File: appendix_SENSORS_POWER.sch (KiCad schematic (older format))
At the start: 18 parts

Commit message: pre Annotation 1
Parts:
- removed C? (x2): 10u, symbol Device:C
- removed R? (x2): 4k7, symbol Device:R
- added C? (x2): 10u, symbol Device:C
- added R? (x3): nc, symbol Device:R
- added R? (x2): 10k, symbol Device:R
- R?: value 4k7 -> 10k
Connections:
- wire segments 81 -> 72
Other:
- note added: "Connectors are missing"
- note added: "select\n- pull-up\n- pull-down"
- note removed: "- Stecker von Tobi\n"
- moved on the sheet: C?, R?

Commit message: 1st annotation, footprints, netlist
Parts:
- C401, C402, C403, C404, C405, C406: renamed from C?; footprint (none) -> Capacitors_SMD:C_0805
- R401, R402, R403, R404, R405, R406, R407, R408, R409, R410, R411, R412: renamed from R?; footprint (none) -> Resistors_SMD:R_0805
- T401, T402, T403: renamed from T?; footprint (none) -> Silicon-Standard:TO-263_D2PAK

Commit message: started layouting TMC2660
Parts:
- C401, C402, C403, C404, C405, C406: footprint Capacitors_SMD:C_0805 -> Capacitors_SMD:C_0603
- R401, R402, R403, R404, R405, R406, R407, R408, R409, R410, R411, R412: footprint Resistors_SMD:R_0805 -> Resistors_SMD:R_0603
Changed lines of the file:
@@
 F 0 "C402" H 4965 1846 50  0000 L CNN
 F 1 "10u" H 4965 1755 50  0000 L CNN
-F 2 "Capacitors_SMD:C_0805" H 4888 1650 50  0001 C CNN
+F 2 "Capacitors_SMD:C_0603" H 4888 1650 50  0001 C CNN
 F 3 "~" H 4850 1800 50  0001 C CNN
 	1    4850 1800
@@
 F 0 "R402" H 4570 1346 50  0000 L CNN
 F 1 "10k" H 4570 1255 50  0000 L CNN
-F 2 "Resistors_SMD:R_0805" V 4430 1300 50  0001 C CNN
+F 2 "Resistors_SMD:R_0603" V 4430 1300 50  0001 C CNN
 F 3 "~" H 4500 1300 50  0001 C CNN
 	1    4500 1300
@@
 F 0 "R404" V 8343 1800 50  0000 C CNN
 F 1 "10k" V 8434 1800 50  0000 C CNN
-F 2 "Resistors_SMD:R_0805" V 8480 1800 50  0001 C CNN
+F 2 "Resistors_SMD:R_0603" V 8480 1800 50  0001 C CNN
 F 3 "~" H 8550 1800 50  0001 C CNN
 	1    8550 1800
@@
 F 0 "R407" V 8343 3150 50  0000 C CNN
 F 1 "10k" V 8434 3150 50  0000 C CNN
-F 2 "Resistors_SMD:R_0805" V 8480 3150 50  0001 C CNN
+F 2 "Resistors_SMD:R_0603" V 8480 3150 50  0001 C CNN
 F 3 "~" H 8550 3150 50  0001 C CNN
 	1    8550 3150
@@
 F 0 "R411" V 8343 4500 50  0000 C CNN
 F 1 "10k" V 8434 4500 50  0000 C CNN
-F 2 "Resistors_SMD:R_0805" V 8480 4500 50  0001 C CNN
+F 2 "Resistors_SMD:R_0603" V 8480 4500 50  0001 C CNN
 F 3 "~" H 8550 4500 50  0001 C CNN
 	1    8550 4500
@@
 F 0 "R403" H 4570 1846 50  0000 L CNN
 F 1 "nc" H 4570 1755 50  0000 L CNN
-F 2 "Resistors_SMD:R_0805" V 4430 1800 50  0001 C CNN
+F 2 "Resistors_SMD:R_0603" V 4430 1800 50  0001 C CNN
 F 3 "~" H 4500 1800 50  0001 C CNN
 	1    4500 1800
@@
 F 0 "R409" H 1820 4346 50  0000 L CNN
 F 1 "4k7" H 1820 4255 50  0000 L CNN
-F 2 "Resistors_SMD:R_0805" V 1680 4300 50  0001 C CNN
+F 2 "Resistors_SMD:R_0603" V 1680 4300 50  0001 C CNN
 F 3 "~" H 1750 4300 50  0001 C CNN
 	1    1750 4300
@@
 F 0 "C405" H 1865 4846 50  0000 L CNN
 F 1 "10u" H 1865 4755 50  0000 L CNN
-F 2 "Capacitors_SMD:C_0805" H 1788 4650 50  0001 C CNN
+F 2 "Capacitors_SMD:C_0603" H 1788 4650 50  0001 C CNN
 F 3 "~" H 1750 4800 50  0001 C CNN
 	1    1750 4800
@@
 F 0 "R405" H 1820 2846 50  0000 L CNN
 F 1 "4k7" H 1820 2755 50  0000 L CNN
-F 2 "Resistors_SMD:R_0805" V 1680 2800 50  0001 C CNN
+F 2 "Resistors_SMD:R_0603" V 1680 2800 50  0001 C CNN
 F 3 "~" H 1750 2800 50  0001 C CNN
 	1    1750 2800
@@
 F 0 "C403" H 1865 3346 50  0000 L CNN
 F 1 "10u" H 1865 3255 50  0000 L CNN
-F 2 "Capacitors_SMD:C_0805" H 1788 3150 50  0001 C CNN
+F 2 "Capacitors_SMD:C_0603" H 1788 3150 50  0001 C CNN
 F 3 "~" H 1750 3300 50  0001 C CNN
 	1    1750 3300
@@
 F 0 "R401" H 1820 1346 50  0000 L CNN
 F 1 "4k7" H 1820 1255 50  0000 L CNN
-F 2 "Resistors_SMD:R_0805" V 1680 1300 50  0001 C CNN
+F 2 "Resistors_SMD:R_0603" V 1680 1300 50  0001 C CNN
 F 3 "~" H 1750 1300 50  0001 C CNN
 	1    1750 1300
@@
 F 0 "C401" H 1865 1846 50  0000 L CNN
 F 1 "10u" H 1865 1755 50  0000 L CNN
-F 2 "Capacitors_SMD:C_0805" H 1788 1650 50  0001 C CNN
+F 2 "Capacitors_SMD:C_0603" H 1788 1650 50  0001 C CNN
 F 3 "~" H 1750 1800 50  0001 C CNN
 	1    1750 1800
@@
 F 0 "C404" H 4965 3346 50  0000 L CNN
 F 1 "10u" H 4965 3255 50  0000 L CNN
-F 2 "Capacitors_SMD:C_0805" H 4888 3150 50  0001 C CNN
+F 2 "Capacitors_SMD:C_0603" H 4888 3150 50  0001 C CNN
 F 3 "~" H 4850 3300 50  0001 C CNN
 	1    4850 3300
@@
 F 0 "R406" H 4570 2846 50  0000 L CNN
 F 1 "10k" H 4570 2755 50  0000 L CNN
-F 2 "Resistors_SMD:R_0805" V 4430 2800 50  0001 C CNN
+F 2 "Resistors_SMD:R_0603" V 4430 2800 50  0001 C CNN
 F 3 "~" H 4500 2800 50  0001 C CNN
 	1    4500 2800
@@
 F 0 "R408" H 4570 3346 50  0000 L CNN
 F 1 "nc" H 4570 3255 50  0000 L CNN
-F 2 "Resistors_SMD:R_0805" V 4430 3300 50  0001 C CNN
+F 2 "Resistors_SMD:R_0603" V 4430 3300 50  0001 C CNN
 F 3 "~" H 4500 3300 50  0001 C CNN
 	1    4500 3300
@@
 F 0 "C406" H 4965 4846 50  0000 L CNN
 F 1 "10u" H 4965 4755 50  0000 L CNN
-F 2 "Capacitors_SMD:C_0805" H 4888 4650 50  0001 C CNN
+F 2 "Capacitors_SMD:C_0603" H 4888 4650 50  0001 C CNN
 F 3 "~" H 4850 4800 50  0001 C CNN
 	1    4850 4800
@@
 F 0 "R410" H 4570 4346 50  0000 L CNN
 F 1 "10k" H 4570 4255 50  0000 L CNN
-F 2 "Resistors_SMD:R_0805" V 4430 4300 50  0001 C CNN
+F 2 "Resistors_SMD:R_0603" V 4430 4300 50  0001 C CNN
 F 3 "~" H 4500 4300 50  0001 C CNN
 	1    4500 4300
@@
 F 0 "R412" H 4570 4846 50  0000 L CNN
 F 1 "nc" H 4570 4755 50  0000 L CNN
-F 2 "Resistors_SMD:R_0805" V 4430 4800 50  0001 C CNN
+F 2 "Resistors_SMD:R_0603" V 4430 4800 50  0001 C CNN
 F 3 "~" H 4500 4800 50  0001 C CNN
 	1    4500 4800

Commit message: Layout: all TMC / Schematic: Oli's comments
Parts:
- added J401, J402, J404, J405, J407, J408, J409, J410: Conn_01x02, Connectors_JST:JST_EH_B02B-EH-A_02x2.50mm_Straight, symbol Connector_Generic:Conn_01x02
- added J403, J406: Screw_Terminal_01x02, Connectors_Terminal_Blocks:TerminalBlock_Altech_AK300-2_P5.00mm, symbol Connector:Screw_Terminal_01x02
- added R413: 10k, Resistors_SMD:R_0603, symbol Device:R
- added R414: nc, Resistors_SMD:R_0603, symbol Device:R
- added T404: BUK963R3-60E, Package_TO_SOT_SMD:TO-263-2, symbol FHNW-Pro4E-FS19T8-Library:BUK963R3-60E
- T401, T402, T403: footprint Silicon-Standard:TO-263_D2PAK -> Package_TO_SOT_SMD:TO-263-2
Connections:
- net labels added: +24V, ADC_Temp_E1, DP_E1, DP_Fan_2, SW_End_Z1_min
- net labels removed: +12V, ADC_Temp_HotEnd, DP_Hotend_1, SW_End_Z_min
- wire segments 72 -> 96
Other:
- note added: "24V on 12V Fan ???"
- note removed: "Connectors are missing"
- note removed: "TODO"
- moved on the sheet: C401, C402, C403, C404, C405, C406, R401, R402, R403, R404, R405, R406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

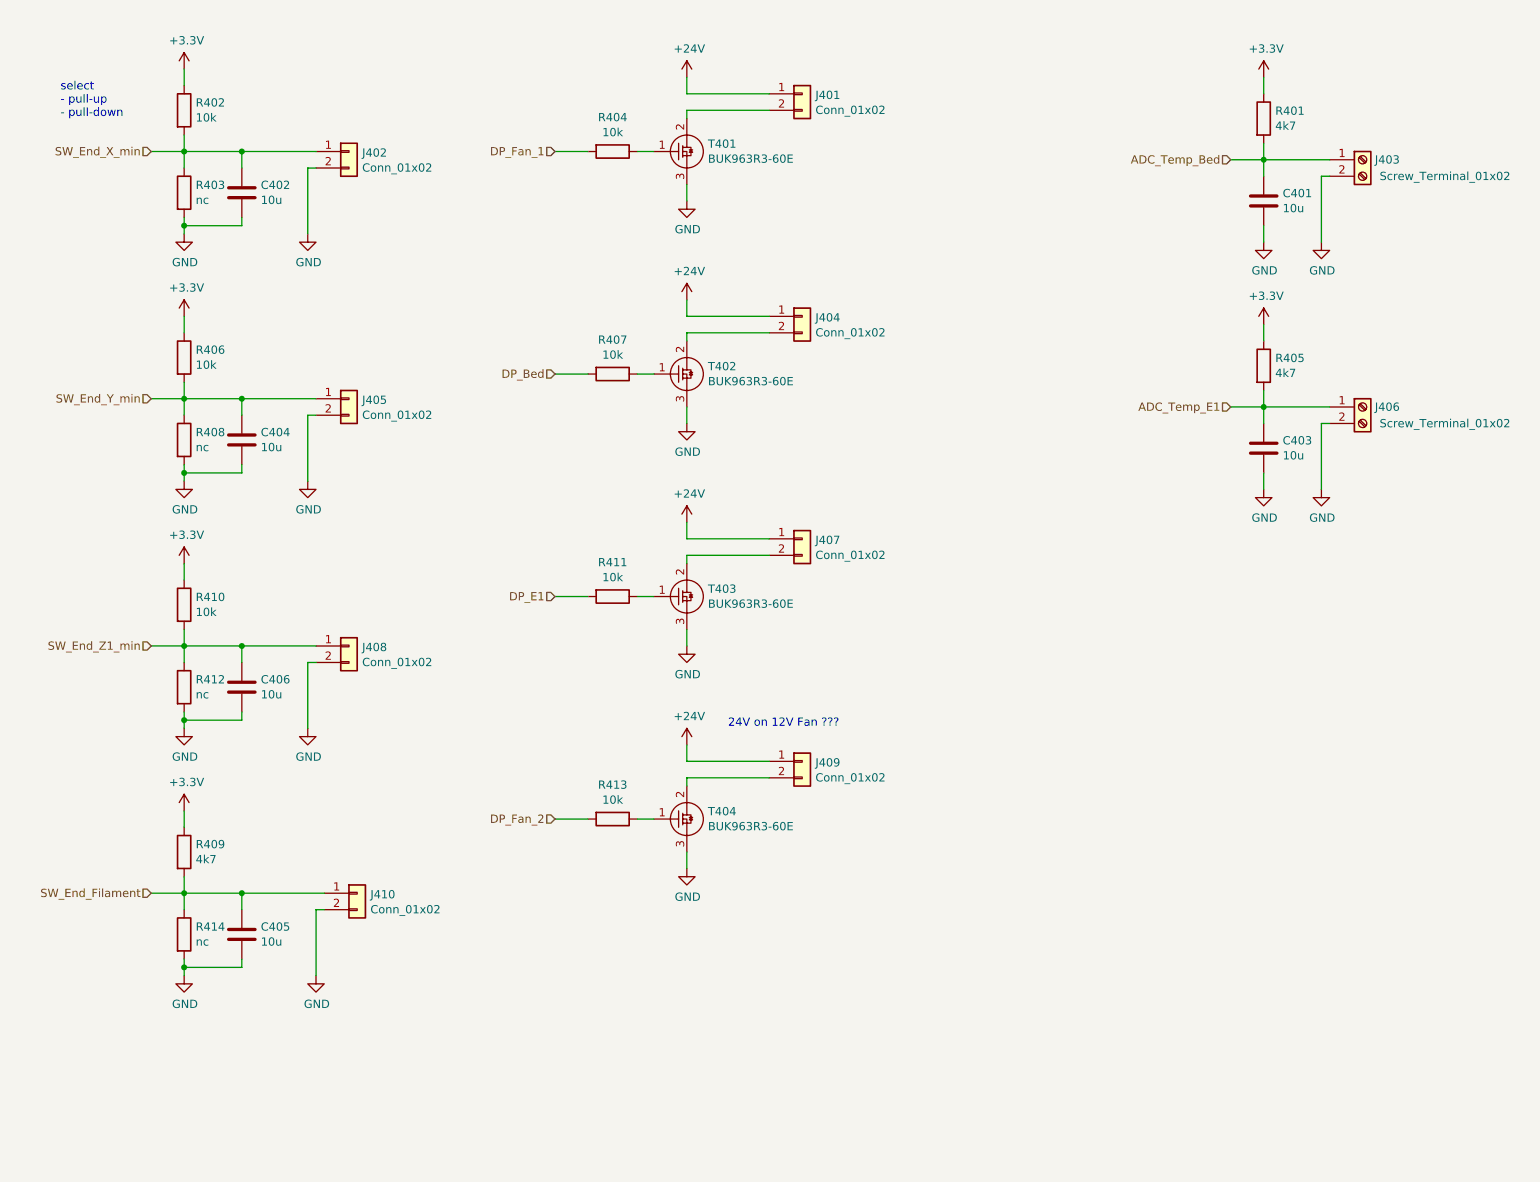
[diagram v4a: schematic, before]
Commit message: added footprints, layouted 3v3 Reg
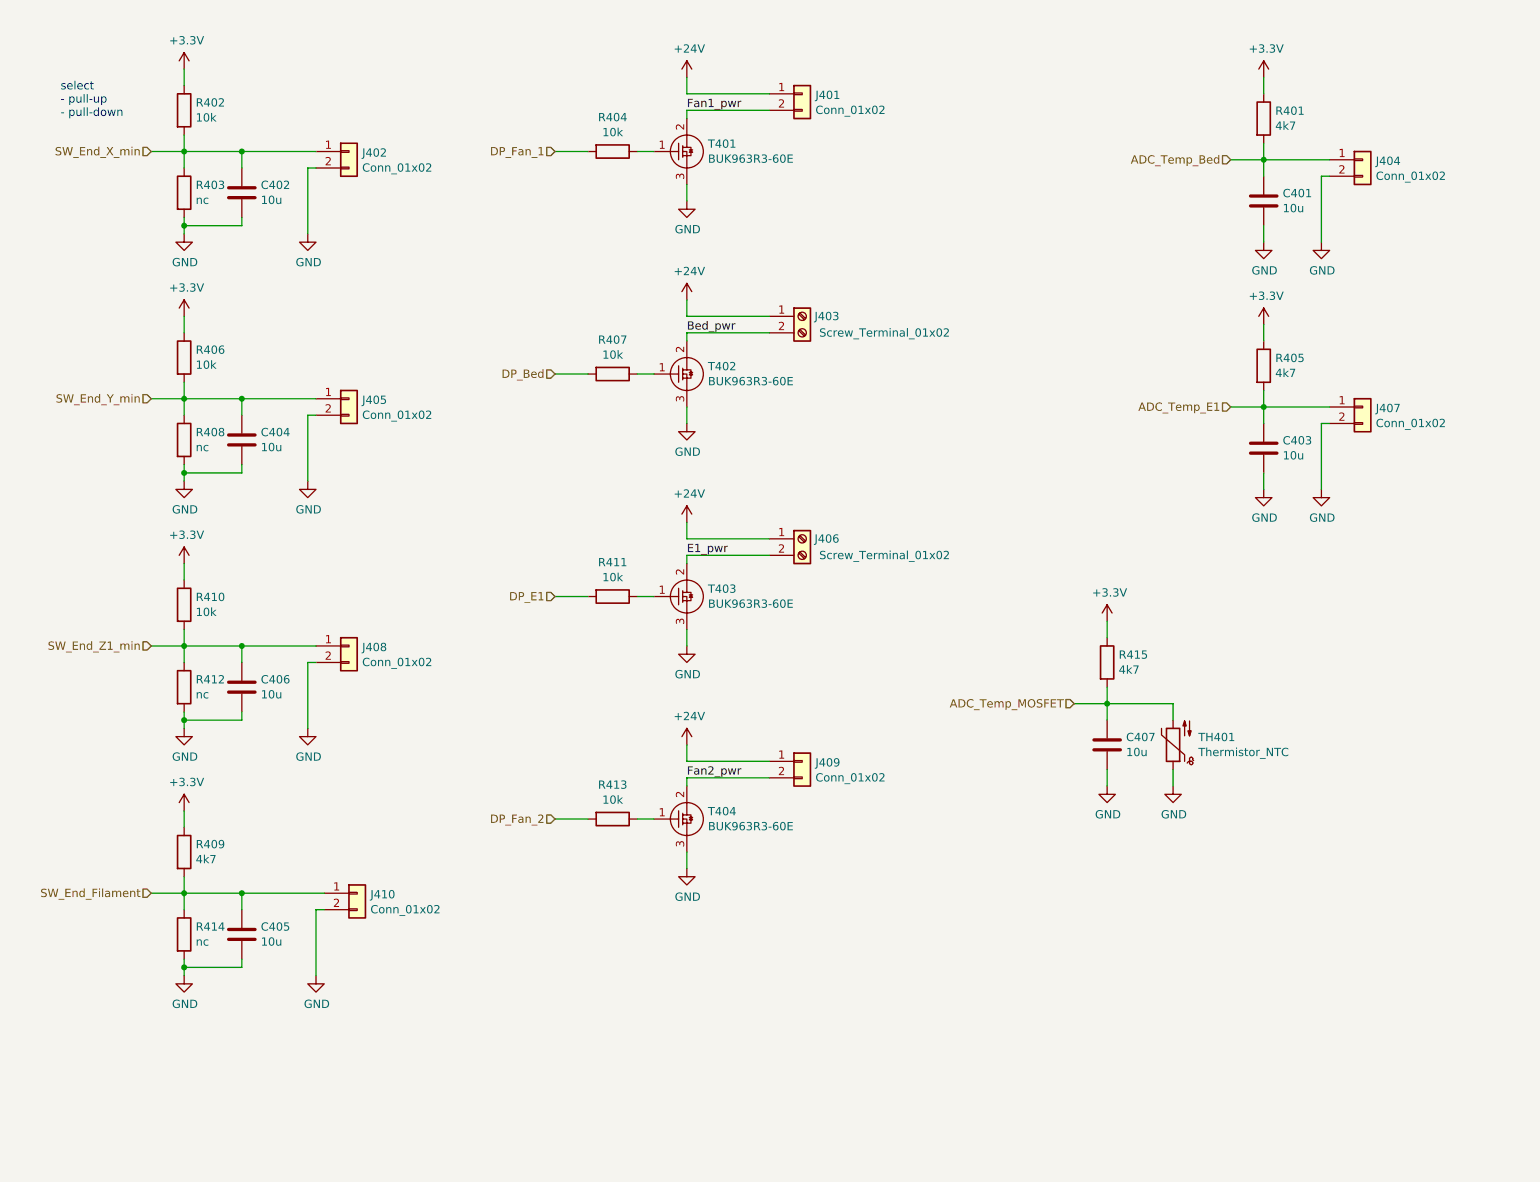
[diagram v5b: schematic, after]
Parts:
- added C407: 10u, Capacitors_SMD:C_0603, symbol Device:C
- added R415: 4k7, Resistors_SMD:R_0603, symbol Device:R
- added TH401: Thermistor_NTC, Resistors_SMD:R_0805_HandSoldering, symbol Device:Thermistor_NTC
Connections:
- net +24V: now also J403.1 (Pin_1), J406.1 (Pin_1); no longer J404.1 (Pin_1), J407.1 (Pin_1)
- net +3V3: now also R415.1
- net ADC_Temp_Bed: now also J404.1 (Pin_1); no longer J403.1 (Pin_1)
- net ADC_Temp_E1: now also J407.1 (Pin_1); no longer J406.1 (Pin_1)
- net GND: now also J404.2 (Pin_2), J407.2 (Pin_2), C407.2, TH401.1; no longer J403.2 (Pin_2), J406.2 (Pin_2)
- net Fan1_pwr: now reaches J401.2 (Pin_2), T401.2
- net Bed_pwr: now reaches T402.2
- net Bed_pwr: now also J403.2 (Pin_2); no longer J404.2 (Pin_2)
- net E1_pwr: now reaches T403.2
- net E1_pwr: now also J406.2 (Pin_2); no longer J407.2 (Pin_2)
- net Fan2_pwr: now reaches J409.2 (Pin_2), T404.2
- new net ADC_Temp_MOSFET: C407.1, R415.2, TH401.2
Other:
- note removed: "24V on 12V Fan ???"
- moved on the sheet: J403, J404, J406, J407

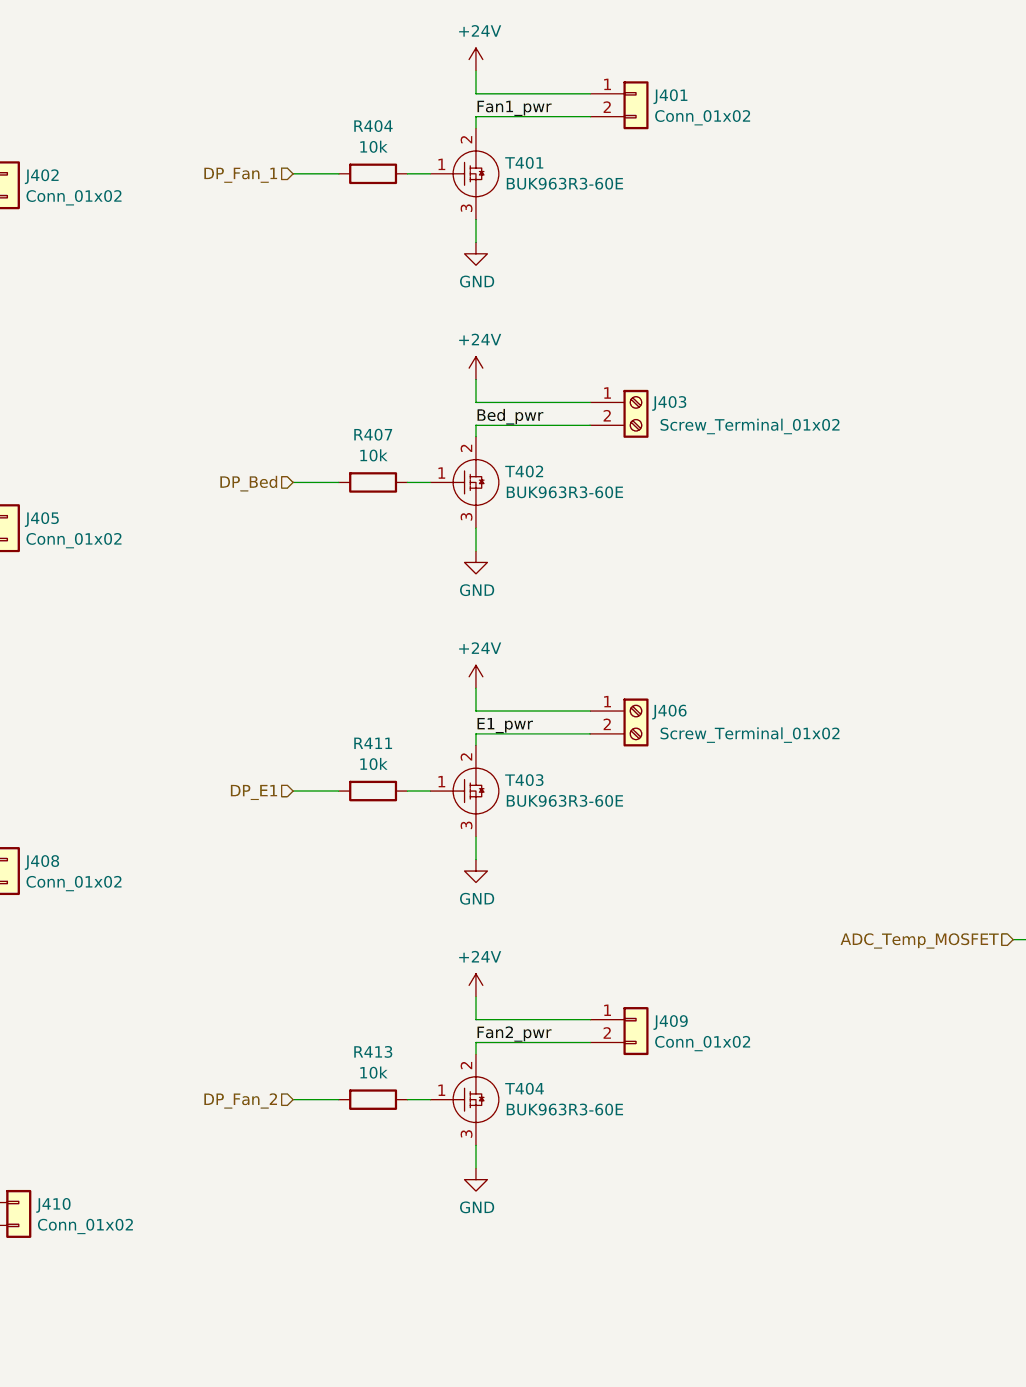
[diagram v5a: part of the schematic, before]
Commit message: added LEDs
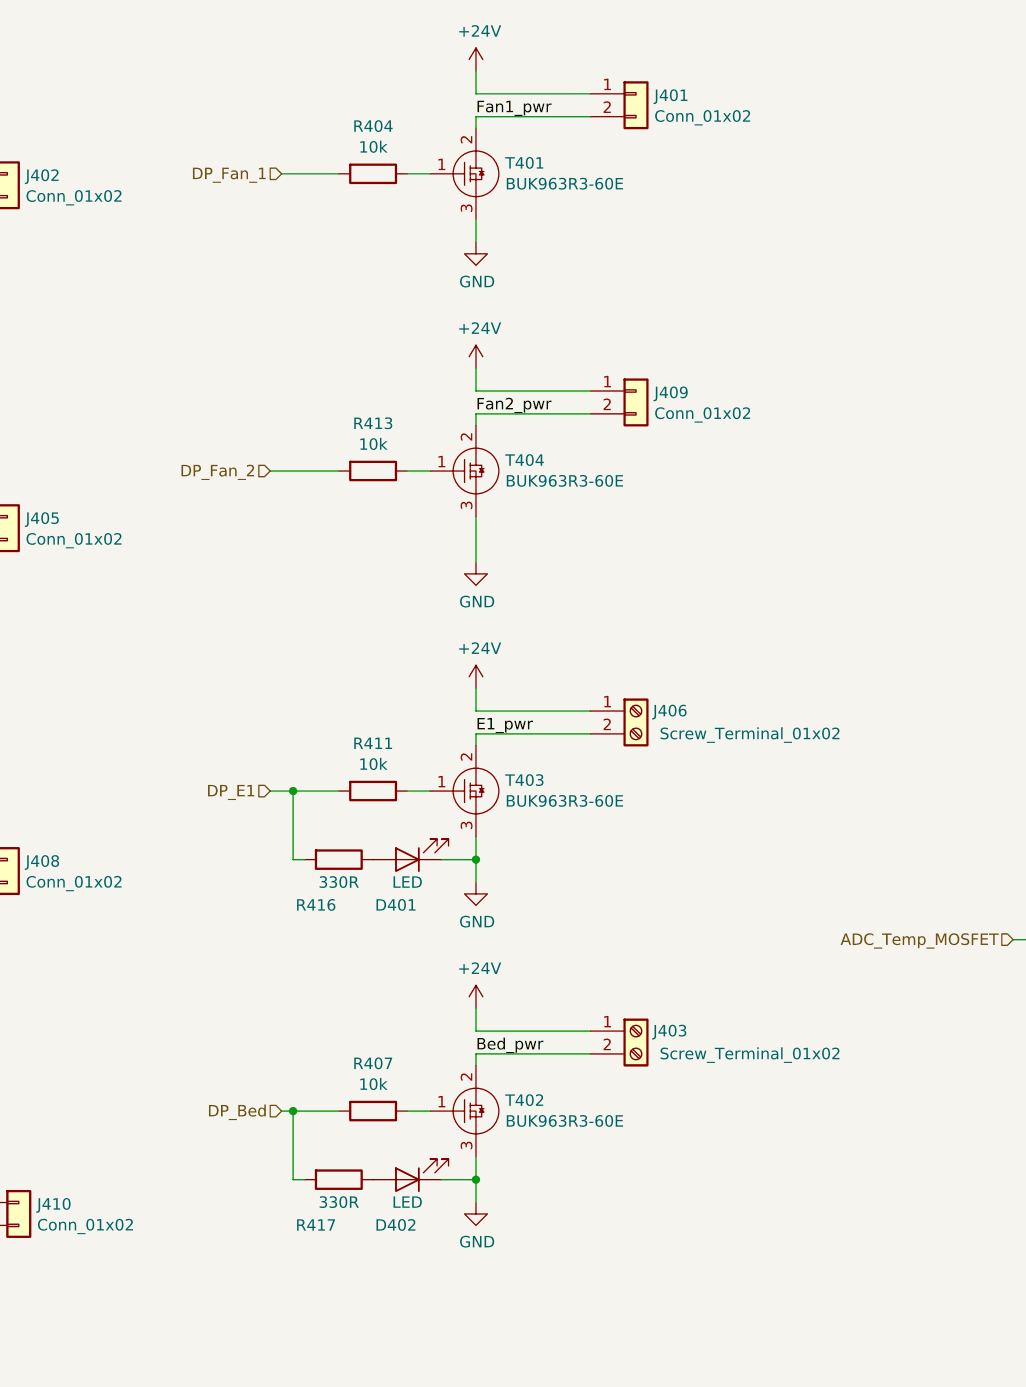
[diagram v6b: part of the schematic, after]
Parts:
- added D401, D402: LED, LED_SMD:LED_0805_2012Metric, symbol Device:LED
- added R416, R417: 330R, Resistors_SMD:R_0603, symbol Device:R
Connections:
- net DP_Bed: now also R417.2
- net DP_E1: now also R416.2
- net GND: now also D401.1 (K), D402.1 (K)
- new net: D401.2 (A), R416.1
- new net: D402.2 (A), R417.1
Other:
- moved on the sheet: J403, J409, R407, R413, T402, T404

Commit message: corrected P.S. Schematic review
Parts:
- added J411: Conn_01x02, Connectors_JST:JST_EH_B02B-EH-A_02x2.50mm_Straight, symbol Connector_Generic:Conn_01x02
- added R418, R419, R421, R422, R423: 100k, Resistors_SMD:R_0603, symbol Device:R
- added R420: 33R, Resistors_SMD:R_0603, symbol Device:R
- added T405: BUK963R3-60E, Package_TO_SOT_SMD:TO-263-2, symbol FHNW-Pro4E-FS19T8-Library:BUK963R3-60E
- R404, R413: value 10k -> 33R
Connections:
- net +24V: now also J411.1 (Pin_1)
- net DP_Bed: now also R423.1
- net DP_E1: now also R422.1
- net DP_Fan_1: now also R418.1
- net DP_Fan_2: now also R419.1
- net GND: now also R418.2, R419.2, R421.2, R422.2, R423.2, T405.3
- new net: R420.1, T405.1
- new net DP_Fan_PCB: R420.2, R421.1
- new net Fan3_pwr: J411.2 (Pin_2), T405.2
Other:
- moved on the sheet: D401, D402, J403, J406, R407, R411, R416, R417, T402, T403
